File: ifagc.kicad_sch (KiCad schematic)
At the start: 39 parts, among them Q901 MMBFJ310, Q902 MMBFJ310, Q903 MMBT3904, Q904 MMBT3904, Q905 BSS138, T901 FT37-43

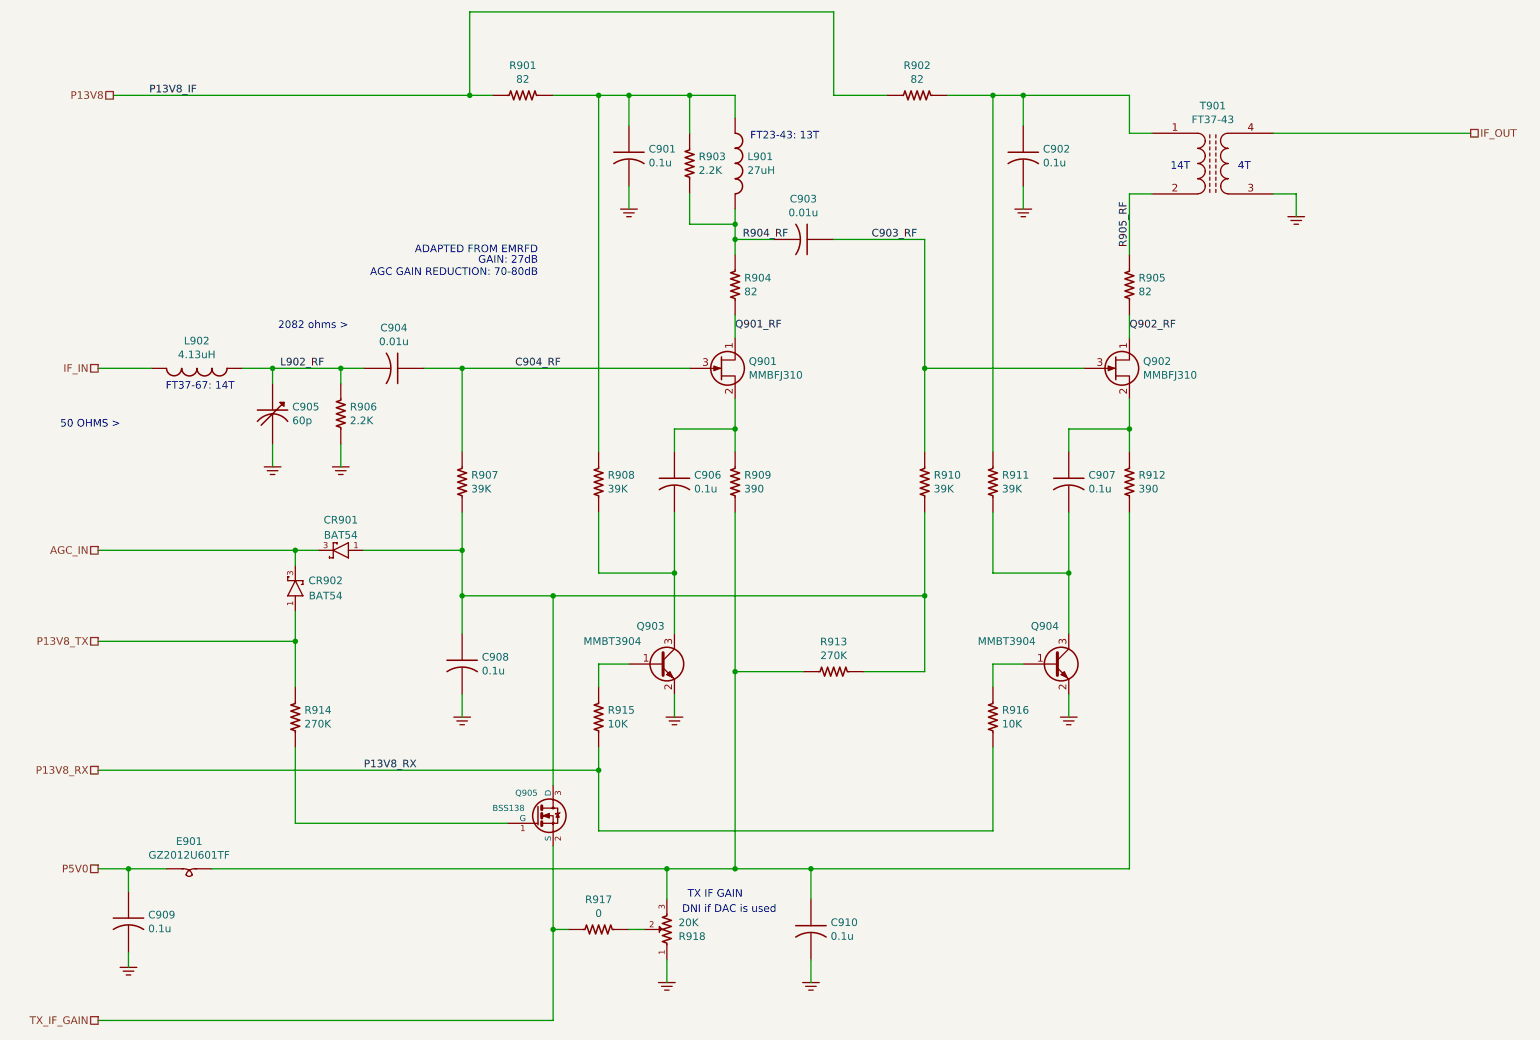
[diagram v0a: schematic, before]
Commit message: Update pcb database to version 6
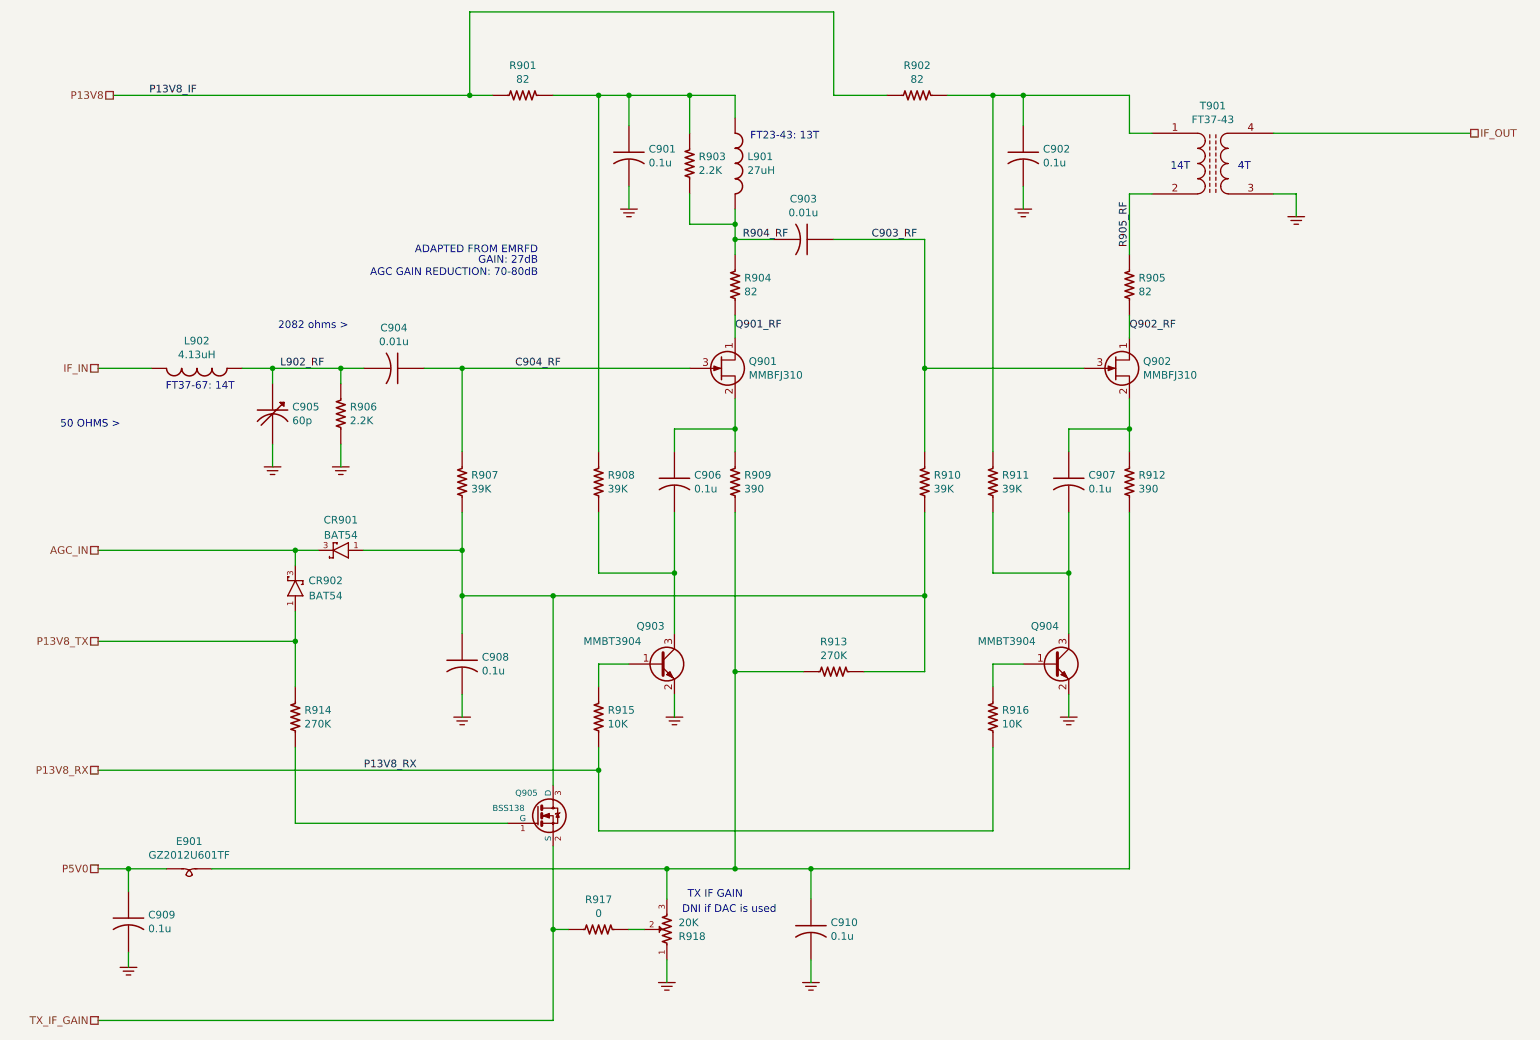
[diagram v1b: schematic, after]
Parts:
- C901, C902, C906, C907, C908, C909, C910: symbol Custom:C_US_0805_0.1UF_X7R_10%_50V_HS -> custom:C_US_0805_0.1UF_X7R_10%_50V_HS
- C903, C904: symbol Custom:C_US_0805_0.1UF_X7R_10%_50V_HS -> custom:C_US_0805_0.1UF_X7R_10%_50V_HS; PartNumber 800238-103 -> 800238-104
- C905: symbol Custom:CVAR_US -> custom:CVAR_US
- CR901, CR902: footprint mods:SOT23-3-SAR -> SOT23; symbol Custom:BAT54 -> custom:BAT54
- E901: footprint Inductor_SMD:L_0805_2012Metric_Pad1.15x1.40mm_HandSolder -> Inductor_SMD:L_0805_2012Metric; symbol Custom:FB0805 -> custom:FB0805; PartNumber 800245-601 -> 80000X-XXX
- L901: symbol Custom:L_US -> custom:L_US; PartNumber 800257-023 -> 8000XX-XXX
- L902: symbol Custom:L_US -> custom:L_US; PartNumber 800276-037 -> 8000XX-XXX
- Q901, Q902: footprint mods:SOT23-3-SAR -> Package_TO_SOT_SMD:SOT-23; symbol Custom:MMBFJ310 -> custom:MMBFJ310
- Q903, Q904: symbol Custom:MMBT3904 -> custom:MMBT3904
- Q905: footprint mods:SOT23-3-SAR -> SOT-23; symbol Custom:BSS138 -> custom:BSS138
- R901, R902, R904, R905: symbol Custom:R_US_0805_1%_HS -> custom:R_US_0805_1%_HS; PartNumber 800235-820 -> 800235-XXX
- R903, R906: symbol Custom:R_US_0805_1%_HS -> custom:R_US_0805_1%_HS; PartNumber 800235-222 -> 800235-XXX
- R907, R908, R910, R911: symbol Custom:R_US_0805_1%_HS -> custom:R_US_0805_1%_HS; PartNumber 800235-393 -> 800235-XXX
- R909, R912: symbol Custom:R_US_0805_1%_HS -> custom:R_US_0805_1%_HS; PartNumber 800235-391 -> 800235-XXX
- R913, R914: symbol Custom:R_US_0805_1%_HS -> custom:R_US_0805_1%_HS; PartNumber 800235-274 -> 800235-XXX
- R915, R916: symbol Custom:R_US_0805_1%_HS -> custom:R_US_0805_1%_HS; PartNumber 800235-103 -> 800235-XXX
- R917: symbol Custom:R_US -> custom:R_US; PartNumber 800235-000 -> 800XXX-XXX
- R918: symbol Custom:POT_US -> custom:POT_US
- T901: symbol Custom:XFMR_RF -> custom:XFMR_RF

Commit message: Sync PCB with schematic
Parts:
- CR901, CR902: footprint SOT23 -> mods:SOT23-3-SAR
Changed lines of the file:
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@@
     (property "Reference" "CR901" (id 0) (at 68.58 101.6 0))
     (property "Value" "BAT54" (id 1) (at 68.58 104.14 0))
-    (property "Footprint" "SOT23" (id 2) (at 68.58 106.68 90)
+    (property "Footprint" "mods:SOT23-3-SAR" (id 2) (at 68.58 106.68 90)
       (effects (font (size 1.524 1.524)) hide)
     )
@@
     (property "Reference" "CR902" (id 0) (at 66.04 111.76 90))
     (property "Value" "BAT54" (id 1) (at 66.04 114.3 90))
-    (property "Footprint" "SOT23" (id 2) (at 60.96 113.03 90)
-      (effects (font (size 1.524 1.524)) hide)
-    )
+    (property "Footprint" "mods:SOT23-3-SAR" (id 2) (at 60.96 113.03 90)
+      (effects (font (size 1.524 1.524)) hide)
+    )

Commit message: Fix BOM part number errors and out of sync footprints which happened during conversion from Kicad 5 to 6
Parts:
- C903, C904: PartNumber 800238-104 -> 800239-103
- E901: PartNumber 80000X-XXX -> 800245-601
- Q901, Q902: footprint Package_TO_SOT_SMD:SOT-23 -> mods:SOT23-3-SAR
- Q905: footprint SOT-23 -> mods:SOT23-3-SAR
- R901, R902, R904, R905: PartNumber 800235-XXX -> 800235-820
- R903, R906: PartNumber 800235-XXX -> 800235-222
- R907, R908, R910, R911: PartNumber 800235-XXX -> 800235-393
- R909, R912: PartNumber 800235-XXX -> 800235-391
- R913, R914: PartNumber 800235-XXX -> 800235-274
- R915, R916: PartNumber 800235-XXX -> 800235-103
- R917: PartNumber 800XXX-XXX -> 800235-000
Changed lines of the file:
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@@
       (effects (font (size 1.524 1.524)))
     )
-    (property "PartNumber" "80000X-XXX" (id 4) (at 42.545 154.305 0)
+    (property "PartNumber" "800245-601" (id 4) (at 42.545 154.305 0)
       (effects (font (size 1.524 1.524)) hide)
     )
@@
       (effects (font (size 1.27 1.27)) (justify left))
     )
-    (property "Footprint" "Package_TO_SOT_SMD:SOT-23" (id 2) (at 137.16 78.105 0)
+    (property "Footprint" "mods:SOT23-3-SAR" (id 2) (at 137.16 78.105 0)
       (effects (font (size 1.27 1.27) italic) (justify left) hide)
     )
@@
       (effects (font (size 1.524 1.524)))
     )
-    (property "PartNumber" "800235-XXX" (id 4) (at 73.152 81.28 90)
+    (property "PartNumber" "800235-222" (id 4) (at 73.152 81.28 90)
       (effects (font (size 1.524 1.524)) hide)
     )
@@
       (effects (font (size 1.524 1.524)))
     )
-    (property "PartNumber" "800238-104" (id 4) (at 91.44 76.2 0)
+    (property "PartNumber" "800239-103" (id 4) (at 91.44 76.2 0)
       (effects (font (size 1.524 1.524)) hide)
     )
@@
       (effects (font (size 1.524 1.524)))
     )
-    (property "PartNumber" "800235-XXX" (id 4) (at 93.472 92.71 90)
+    (property "PartNumber" "800235-393" (id 4) (at 93.472 92.71 90)
       (effects (font (size 1.524 1.524)) hide)
     )
@@
       (effects (font (size 1.016 1.016)) (justify left))
     )
-    (property "Footprint" "SOT-23" (id 2) (at 98.298 148.5392 0)
+    (property "Footprint" "mods:SOT23-3-SAR" (id 2) (at 98.298 148.5392 0)
       (effects (font (size 0.7366 0.7366)) hide)
     )
@@
       (effects (font (size 1.524 1.524)))
     )
-    (property "PartNumber" "800235-XXX" (id 4) (at 65.532 132.08 90)
+    (property "PartNumber" "800235-274" (id 4) (at 65.532 132.08 90)
       (effects (font (size 1.524 1.524)) hide)
     )
@@
       (effects (font (size 1.524 1.524)))
     )
-    (property "PartNumber" "800235-XXX" (id 4) (at 116.332 132.08 90)
+    (property "PartNumber" "800235-103" (id 4) (at 116.332 132.08 90)
       (effects (font (size 1.524 1.524)) hide)
     )
@@
       (effects (font (size 1.524 1.524)))
     )
-    (property "PartNumber" "800235-XXX" (id 4) (at 139.192 92.71 90)
+    (property "PartNumber" "800235-391" (id 4) (at 139.192 92.71 90)
       (effects (font (size 1.524 1.524)) hide)
     )
@@
       (effects (font (size 1.524 1.524)))
     )
-    (property "PartNumber" "800235-XXX" (id 4) (at 116.332 92.71 90)
+    (property "PartNumber" "800235-393" (id 4) (at 116.332 92.71 90)
       (effects (font (size 1.524 1.524)) hide)
     )
@@
       (effects (font (size 1.524 1.524)))
     )
-    (property "PartNumber" "800235-XXX" (id 4) (at 139.192 59.69 90)
+    (property "PartNumber" "800235-820" (id 4) (at 139.192 59.69 90)
       (effects (font (size 1.524 1.524)) hide)
     )
@@
       (effects (font (size 1.524 1.524)))
     )
-    (property "PartNumber" "800235-XXX" (id 4) (at 131.572 39.37 90)
+    (property "PartNumber" "800235-222" (id 4) (at 131.572 39.37 90)
       (effects (font (size 1.524 1.524)) hide)
     )
@@
       (effects (font (size 1.524 1.524)))
     )
-    (property "PartNumber" "800235-XXX" (id 4) (at 101.6 35.052 90)
+    (property "PartNumber" "800235-820" (id 4) (at 101.6 35.052 90)
       (effects (font (size 1.524 1.524)) hide)
     )
@@
       (effects (font (size 1.524 1.524)))
     )
-    (property "PartNumber" "800238-104" (id 4) (at 160.02 54.61 0)
+    (property "PartNumber" "800239-103" (id 4) (at 160.02 54.61 0)
       (effects (font (size 1.524 1.524)) hide)
     )
@@
       (effects (font (size 1.27 1.27)) (justify left))
     )
-    (property "Footprint" "Package_TO_SOT_SMD:SOT-23" (id 2) (at 203.2 78.105 0)
+    (property "Footprint" "mods:SOT23-3-SAR" (id 2) (at 203.2 78.105 0)
       (effects (font (size 1.27 1.27) italic) (justify left) hide)
     )
@@
       (effects (font (size 1.524 1.524)))
     )
-    (property "PartNumber" "800235-XXX" (id 4) (at 182.372 132.08 90)
+    (property "PartNumber" "800235-103" (id 4) (at 182.372 132.08 90)
       (effects (font (size 1.524 1.524)) hide)
     )
@@
       (effects (font (size 1.524 1.524)))
     )
-    (property "PartNumber" "800235-XXX" (id 4) (at 205.232 92.71 90)
+    (property "PartNumber" "800235-391" (id 4) (at 205.232 92.71 90)
       (effects (font (size 1.524 1.524)) hide)
     )
@@
       (effects (font (size 1.524 1.524)))
     )
-    (property "PartNumber" "800235-XXX" (id 4) (at 182.372 92.71 90)
+    (property "PartNumber" "800235-393" (id 4) (at 182.372 92.71 90)
       (effects (font (size 1.524 1.524)) hide)
     )
@@
       (effects (font (size 1.524 1.524)))
     )
-    (property "PartNumber" "800235-XXX" (id 4) (at 205.232 59.69 90)
+    (property "PartNumber" "800235-820" (id 4) (at 205.232 59.69 90)
       (effects (font (size 1.524 1.524)) hide)
     )
@@
       (effects (font (size 1.524 1.524)))
     )
-    (property "PartNumber" "800235-XXX" (id 4) (at 167.64 35.052 90)
+    (property "PartNumber" "800235-820" (id 4) (at 167.64 35.052 90)
       (effects (font (size 1.524 1.524)) hide)
     )
@@
       (effects (font (size 1.524 1.524)))
     )
-    (property "PartNumber" "800235-XXX" (id 4) (at 170.942 92.71 90)
+    (property "PartNumber" "800235-393" (id 4) (at 170.942 92.71 90)
       (effects (font (size 1.524 1.524)) hide)
     )
@@
       (effects (font (size 1.524 1.524)))
     )
-    (property "PartNumber" "800235-XXX" (id 4) (at 153.67 131.572 90)
+    (property "PartNumber" "800235-274" (id 4) (at 153.67 131.572 90)
       (effects (font (size 1.524 1.524)) hide)
     )
@@
       (effects (font (size 1.524 1.524)))
     )
-    (property "PartNumber" "800XXX-XXX" (id 4) (at 114.3 174.752 90)
-      (effects (font (size 1.524 1.524)) hide)
-    )
+    (property "PartNumber" "800235-000" (id 4) (at 114.3 174.752 90)
+      (effects (font (size 1.524 1.524)) hide)
+    )
